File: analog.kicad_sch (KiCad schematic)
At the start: 13 parts, among them J2 73100-0105, K1 AQY210EHA

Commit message: analog
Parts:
- removed R?: (no value), symbol Device:R_Small
- removed U?: (no value), symbol Amplifier_Operational:OPA356xxD
- removed U?: LM27762, Package_SON:WSON-12-1EP_3x2mm_P0.5mm_EP1x2.65_ThermalVias, symbol Regulator_SwitchedCapacitor:LM27762
- added C34, C36, C39, C40: (no value), symbol Device:C_Small
- added C37: (no value), symbol Device:C_Variable
- added D4, D5: (no value), symbol Device:D_Schottky
- added IC10, IC9: (no value), symbol project_library:MCP6S91-E_MS
- added J4: (no value), symbol project_library:73100-0105
- added K3: (no value), symbol project_library:AQY210EHA
- added R16, R17, R19, R21, R27, R28: (no value), symbol Device:R
- added R24, R25, R26: (no value), symbol Device:R_Small
- added TP1, TP2, TP3, TP4: (no value), symbol Connector:TestPoint
- added U10, U11, U9: (no value), symbol Amplifier_Operational:MCP6022
- C30: value 100n -> (none); footprint Capacitor_SMD:C_0805_2012Metric_Pad1.18x1.45mm_HandSolder -> (none)
- J2: value 73100-0105 -> (none); footprint 73100-0105 -> (none)
- K1: value AQY210EHA -> (none); footprint project_library:AQY210EHAX -> (none)
- R18: value 1k -> (none); footprint Resistor_SMD:R_0805_2012Metric_Pad1.20x1.40mm_HandSolder -> (none)
- R20: value 835k -> (none); footprint Resistor_SMD:R_0805_2012Metric_Pad1.20x1.40mm_HandSolder -> (none)
- R22: value 165k -> (none); footprint Resistor_SMD:R_0805_2012Metric_Pad1.20x1.40mm_HandSolder -> (none)
- gave numbers to parts that had none: 3
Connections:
- net +3.3VA: now also D4.1 (K), IC10.8 (VDD), IC9.8 (VDD), U10.8 (V+), U11.8 (V+), U9.8 (V+)
- net -3V3: now also IC10.4 (VSS), IC9.4 (VSS); no longer D7.2 (A)
- net GND: now also R24.1
- net GNDA: now also C39.2, C40.2, U10.4 (V-), U11.4 (V-), U9.4 (V-); no longer C38.2, J2.1, J2.2, R22.2
- net at C32.1, C38.1, D6.2 (A)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: now also U10.3 (+)
- net CH1_Gnd_Sel renamed ch1_coupling_sel
- new net: C36.1, C37.1, D4.2 (A), D5.1 (K), R25.1, R26.1, U9.3 (+)
- new net: R21.1, U11.7
- new net: IC10.2 (CH0), TP2.1, U10.1, U10.2 (-)
- new net: C40.1, R28.1, U9.5 (+)
- new net: IC10.3 (VREF), U10.6 (-), U10.7
- new net: C34.1, C36.2, K3.3 (SW), R25.2
- new net: R16.2, U11.3 (+)
- new net: IC9.2 (CH0), TP1.1, U9.1, U9.2 (-)
- new net: IC9.3 (VREF), U9.6 (-), U9.7
- new net: R19.1, U11.1
- new net: R17.2, U11.5 (+)
- new net: K3.2 (Kathode), R24.2
- new net: C34.2, J4.3, K3.4 (SW)
- new net: C39.1, R27.1, U10.5 (+)
- new net Analog_Out_CH1: IC10.1 (VOUT), TP4.1
- new net Analog_Out_CH2: IC9.1 (VOUT), TP3.1
- new net GNDREF: C37.2, C38.2, D5.2 (A), D7.2 (A), J2.1, J2.2, J4.1, J4.2, R22.2, R26.2
- new net Offset_Pwm_CH1: R27.2
- new net Offset_Pwm_CH2: R28.2
- new net Trigger_CH1: R19.2
- new net Trigger_CH2: R21.2
- new net Trigger_Ref: U11.2 (-), U11.6 (-)
- new net analog_out_ch1: R16.1
- new net analog_out_ch2: R17.1
- new net ch2_coupling_sel: K3.1 (Anode)
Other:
- note added: "CHANNEL1"
- note added: "CHANNEL2"
- note added: "Trigger"
- moved on the sheet: C30, C32, C38, D6, D7, J2, K1, R18, R20, R22

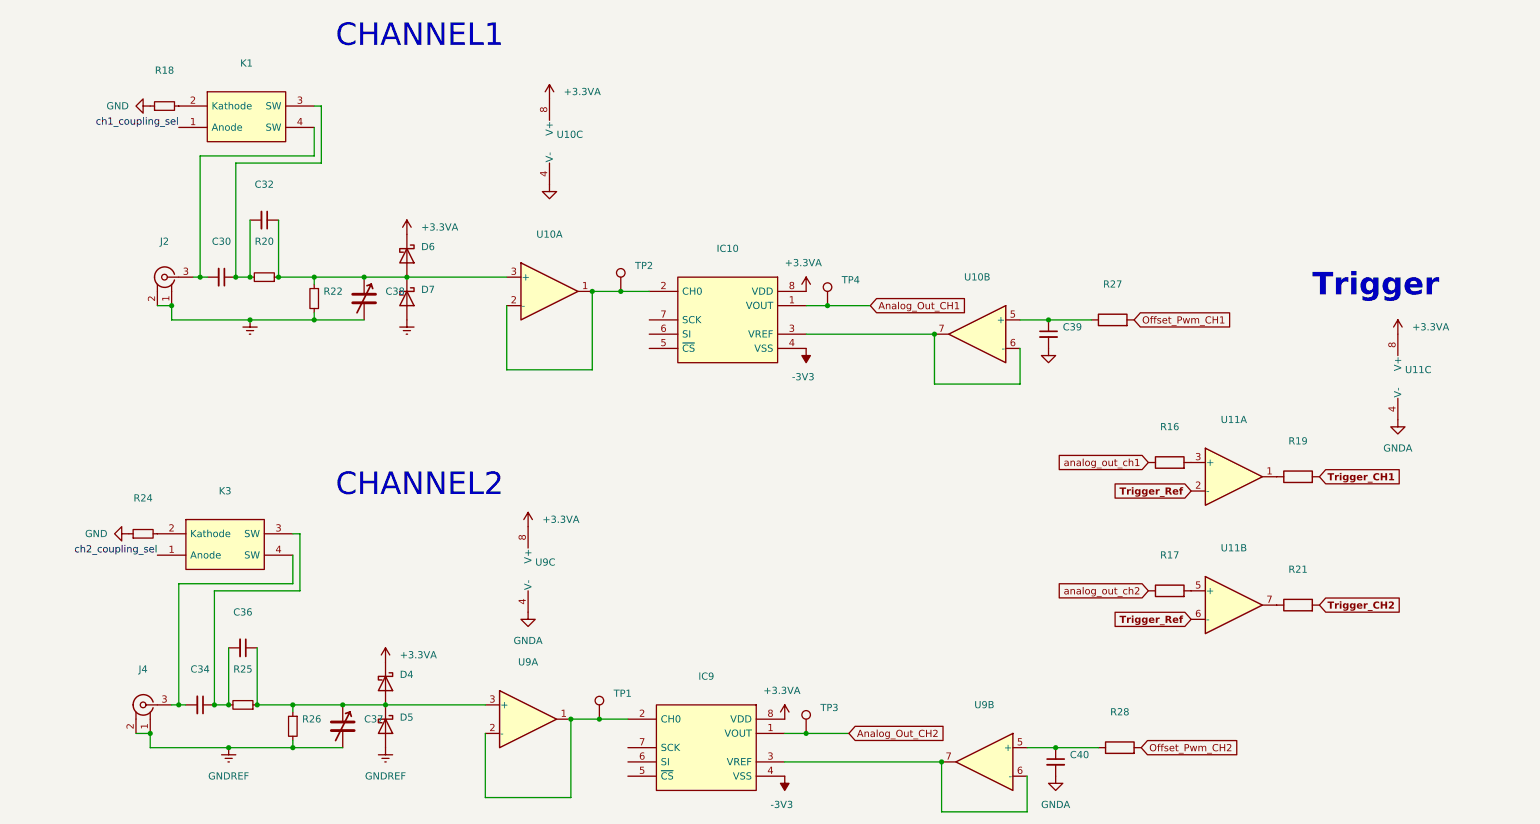
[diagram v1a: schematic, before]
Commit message: resolve DRC on schematic
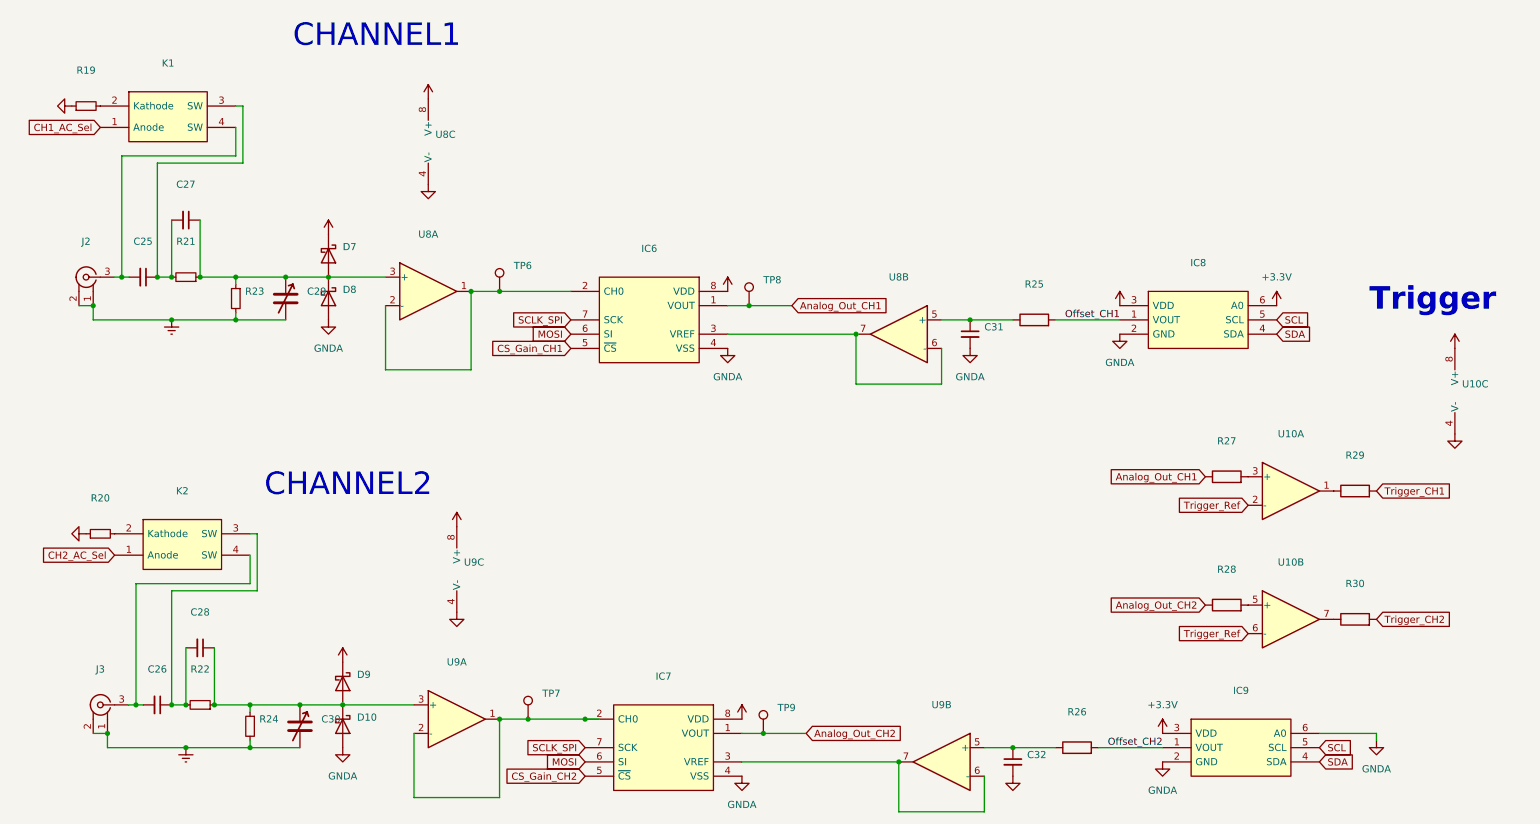
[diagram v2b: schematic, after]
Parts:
- added IC8, IC9: (no value), symbol project_library:DAC5571IDBVR
- renumbered C30 to C25, C34 to C26, C32 to C27, C36 to C28, C38 to C29, C37 to C30, C39 to C31, C40 to C32, D5 to D10, D6 to D7, D7 to D8, D4 to D9, IC10 to IC6, IC9 to IC7, J4 to J3, K3 to K2, R18 to R19, R24 to R20, R20 to R21, R25 to R22, R22 to R23, R26 to R24, R27 to R25, R28 to R26, R16 to R27, R17 to R28, R19 to R29, R21 to R30, TP2 to TP6, TP1 to TP7, TP4 to TP8, TP3 to TP9, U11 to U10, U10 to U8
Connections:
- net -3V3 is gone; now on net GNDA: IC6.4 (VSS), IC7.4 (VSS)
- net analog_out_ch1 is gone; now on net Analog_Out_CH1: R27.1
- net analog_out_ch2 is gone; now on net Analog_Out_CH2: R28.1
- net GNDA: now also D10.2 (A), D8.2 (A), IC8.2 (GND), IC9.2 (GND), IC9.6 (A0)
- net GNDREF: no longer D10.2 (A), D8.2 (A)
- net CS_Gain_CH1: now reaches IC6.5 (~{CS})
- net MOSI: now reaches IC6.6 (SI)
- net MOSI: now also IC7.6 (SI)
- net SCLK_SPI: now reaches IC6.7 (SCK)
- net SCLK_SPI: now also IC7.7 (SCK)
- net CS_Gain_CH2: now reaches IC7.5 (~{CS})
- net Offset_Pwm_CH1 renamed Offset_CH1
- net Offset_CH1: now also IC8.1 (VOUT)
- net Offset_Pwm_CH2 renamed Offset_CH2
- net Offset_CH2: now also IC9.1 (VOUT)
- net ch1_coupling_sel renamed CH1_AC_Sel
- net ch2_coupling_sel renamed CH2_AC_Sel
- new net +3V3: IC8.3 (VDD), IC8.6 (A0), IC9.3 (VDD)
- new net SCL: IC8.5 (SCL), IC9.5 (SCL)
- new net SDA: IC8.4 (SDA), IC9.4 (SDA)
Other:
- moved on the sheet: C25, C26, C27, C28, C29, C30, C31, C32, D10, D7, D8, D9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
